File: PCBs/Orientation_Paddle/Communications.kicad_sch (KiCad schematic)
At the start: 18 parts

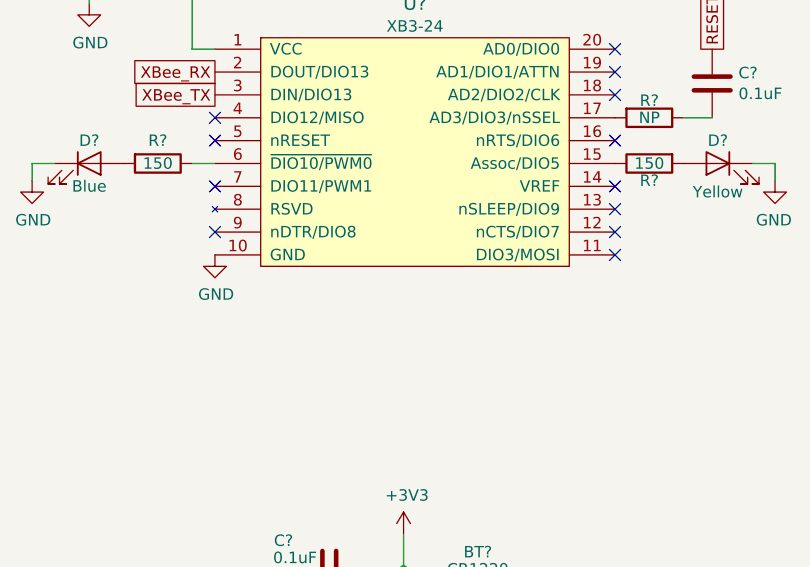
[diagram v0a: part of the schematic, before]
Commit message: Updated Ori. Paddle Schematic with Final Revisions
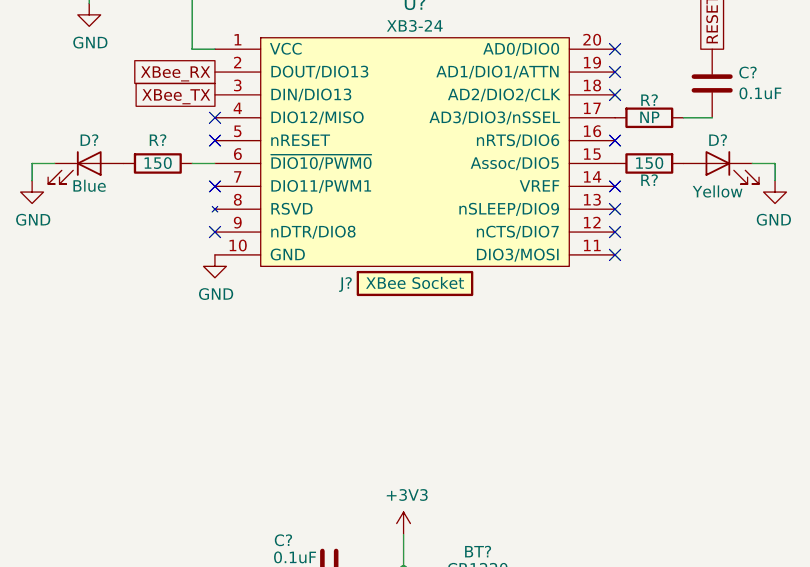
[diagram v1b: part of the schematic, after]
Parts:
- added J?: 1-0000050, connectors:1-0000050, symbol connectors:1-0000050
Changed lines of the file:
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@@
     (pin "2")
+  )
+  (symbol (lib_id "connectors:1-0000050") (at 83.185 83.82 0) (unit 1)
+    (in_bom yes) (on_board yes)
+    (property "Reference" "J?" (id 0) (at 75.565 83.82 0))
+    (property "Value" "1-0000050" (id 1) (at 84.455 83.82 0)
+      (effects (font (size 1.27 1.27)) hide)
+    )
+    (property "Footprint" "connectors:1-0000050" (id 2) (at 83.185 83.82 0)
+      (effects (font (size 1.27 1.27)) hide)
+    )
+    (property "Datasheet" "~" (id 3) (at 83.185 83.82 90)
+      (effects (font (size 1.27 1.27)) hide)
+    )
+    (property "Internal Part Number" "1-0000050" (id 4) (at 83.185 83.82 0)
+      (effects (font (size 1.27 1.27)) hide)
+    )
+    (property "Populated" "1" (id 5) (at 83.185 83.82 90)
+      (effects (font (size 1.27 1.27)) hide)
+    )
+    (property "PValue" "XBee Socket" (id 6) (at 83.185 83.82 0))
   )
   (symbol (lib_id "power:GND") (at 123.19 72.39 0) (mirror y) (unit 1)

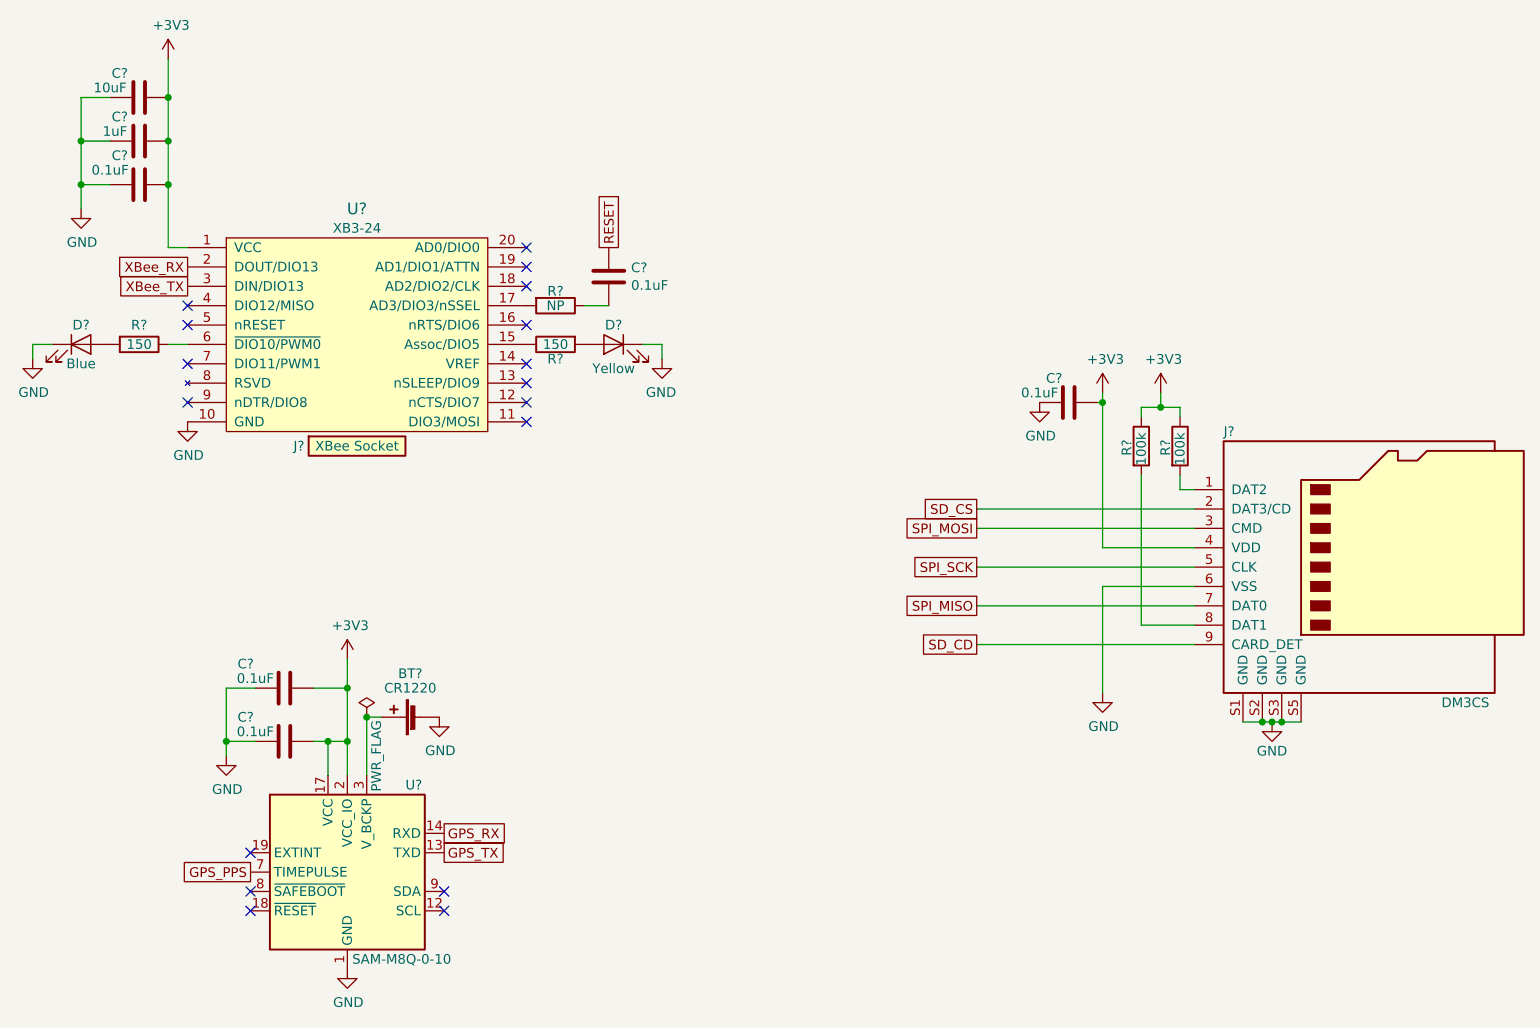
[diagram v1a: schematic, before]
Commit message: Orientation Paddle Initial PCB Layout
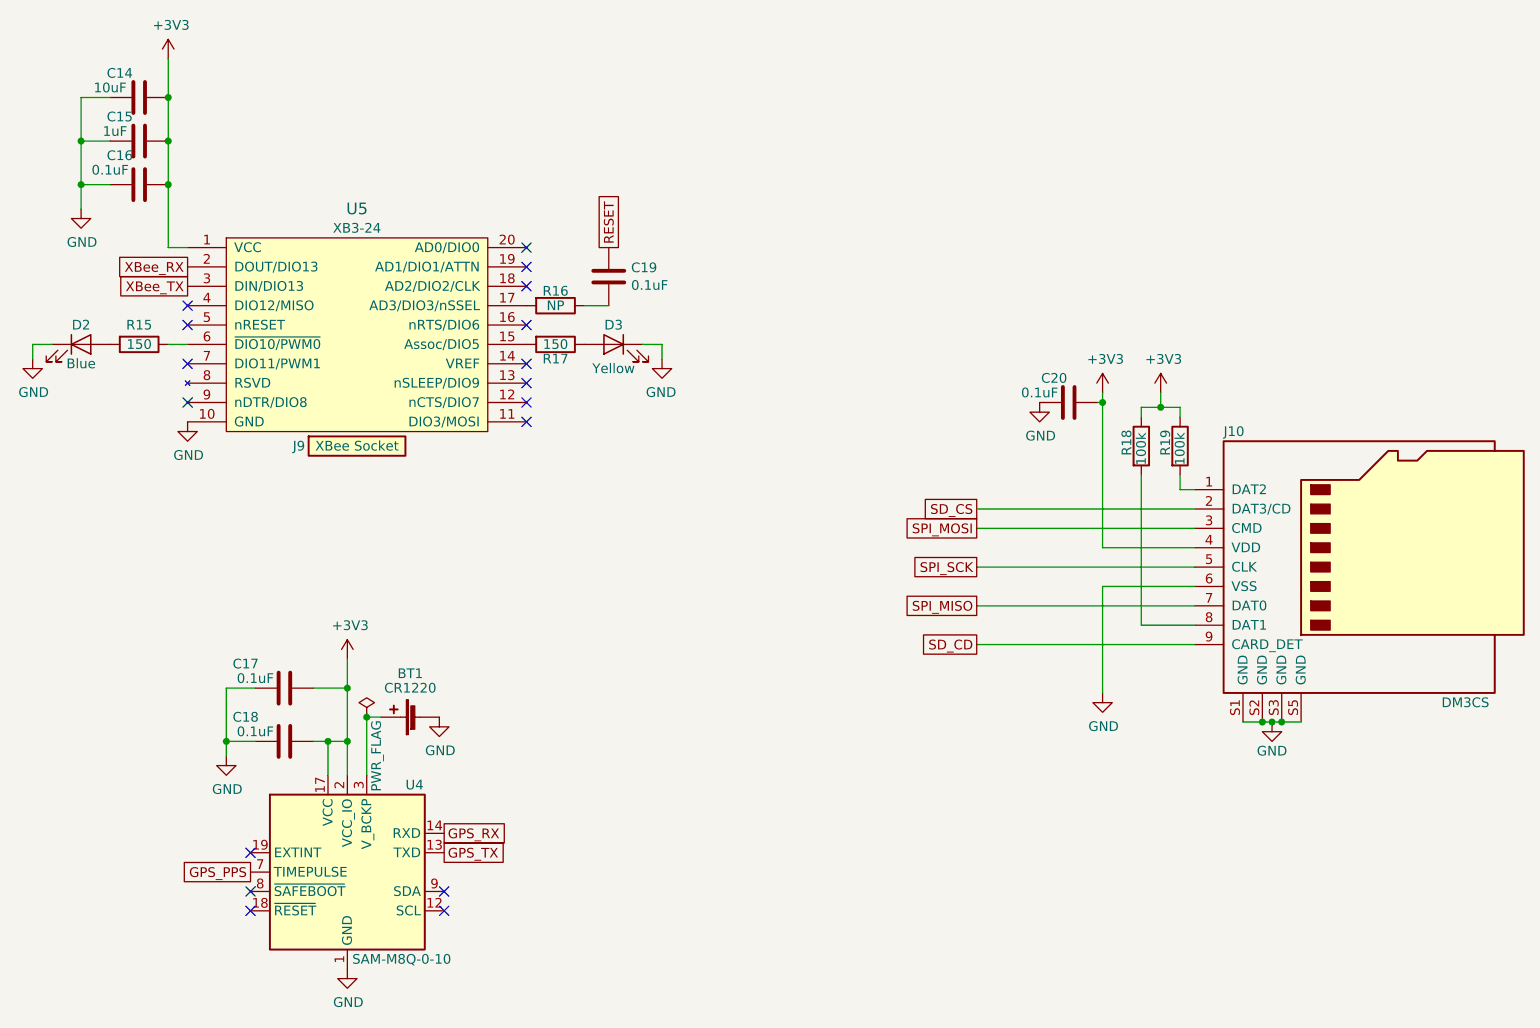
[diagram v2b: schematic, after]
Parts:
- J10: renamed from J?; footprint (none) -> connectors:1-0000190
- gave numbers to parts that had none: 18
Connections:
- net at U5.15 (Assoc/DIO5): now also R17.2; no longer R17.1
- net at D3.2 (A): now also R17.1; no longer R17.2
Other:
- moved on the sheet: R17
